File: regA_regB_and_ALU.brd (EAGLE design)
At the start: 100 x 100 mm, 29 parts

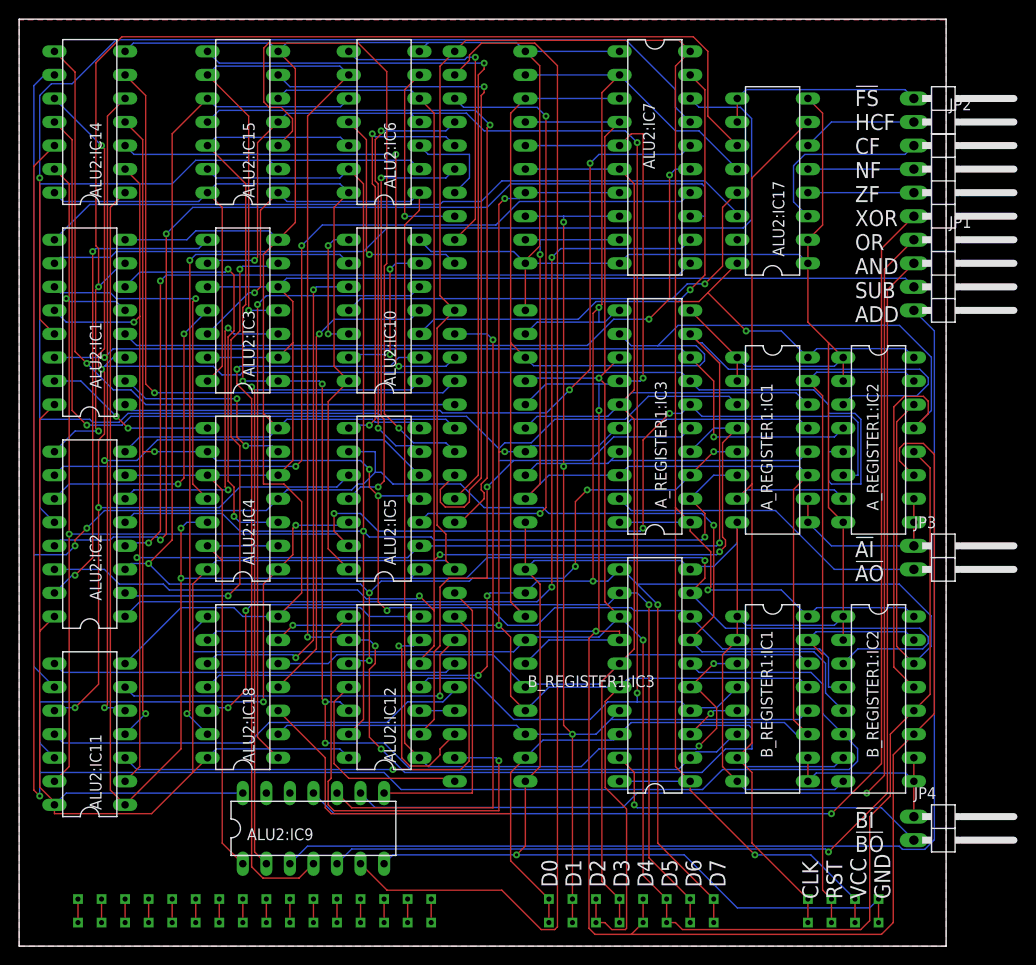
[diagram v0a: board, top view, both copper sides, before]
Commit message: Finished all moduled except Logic Control Unit and modified ALU logic
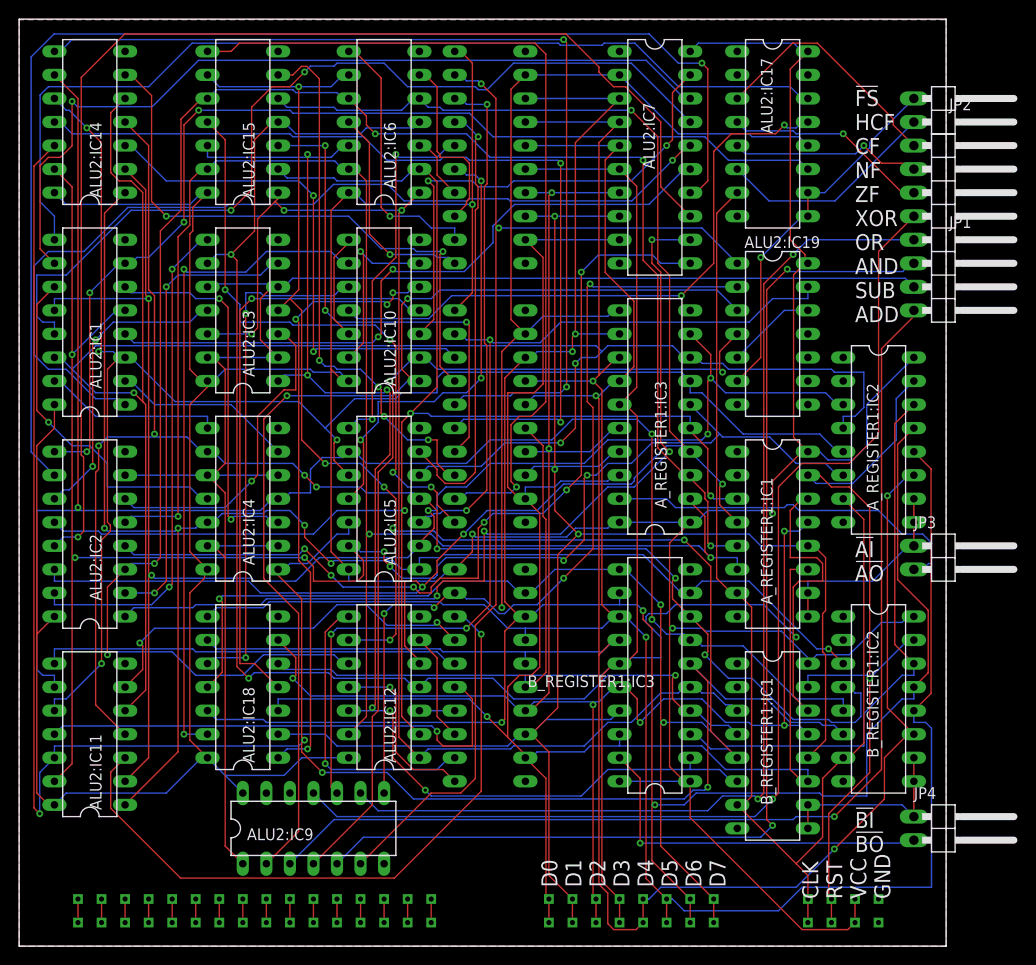
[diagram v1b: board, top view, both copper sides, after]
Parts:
- added ALU2:IC19: 74LS11N, 74xx-eu:DIL14
- moved A_REGISTER1:IC1 10.2 mm to (-31.8, 45.7)
- moved ALU2:IC17 5.08 mm to (-31.8, 88.9), turned to 270 degrees
- moved B_REGISTER1:IC1 5.08 mm to (-31.8, 22.9)
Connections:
- new net ALU2:N$56: ALU2:IC19.12, ALU2:IC19.5
- net !FS: now also ALU2:IC19.6
- net ALU2:N$26: now also ALU2:IC19.3
- net ALU2:N$27: now also ALU2:IC19.4
- net ALU2:N$29: now also ALU2:IC19.1
- net ALU2:N$38: now also ALU2:IC19.2
- net ALU2:N$47: now also ALU2:IC19.13
- net GND: now also ALU2:IC19.7
- net VCC: now also ALU2:IC19.14
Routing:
- net GND: track 550.3 -> 0.00 mm, vias 1 -> 0
- net ALU2:N$38: track 31.9 -> 91.9 mm, vias 0 -> 4
- net N$52: track 220.5 -> 163.3 mm, vias 1 -> 3
- net ALU2:N$26: track 70.7 -> 116.9 mm, vias 1 -> 2
- net N$64: track 204.3 -> 161.0 mm, vias 3 -> 5
- net ALU2:N$2: track 94.8 -> 136.3 mm, vias 2 -> 1
- net N$50: track 156.5 -> 193.8 mm, vias 6 -> 5
- net DATA_3: track 189.3 -> 225.3 mm, vias 0 -> 1
- net DATA_4: track 267.8 -> 233.1 mm
- net ALU2:N$47: track 72.4 -> 106.2 mm, vias 1 -> 3
- net N$54: track 203.8 -> 170.2 mm
- net DATA_6: track 276.0 -> 243.9 mm, vias 3 -> 5
- net N$58: track 186.2 -> 154.1 mm, vias 5 -> 6
- net ALU2:N$41: track 76.6 -> 105.9 mm, vias 1 -> 2
- net N$61: track 249.6 -> 220.3 mm, vias 3 -> 4
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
